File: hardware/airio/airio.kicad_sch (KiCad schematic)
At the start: 21 parts, among them J1 LiPo 1S, J2 GPS, J3 SCREEN, J4 I2C, SW1 TS-1187A-B-A-B, U1 XIAO nRF52840 Plus, U2 BMP581, U3 LSM6DSV16X

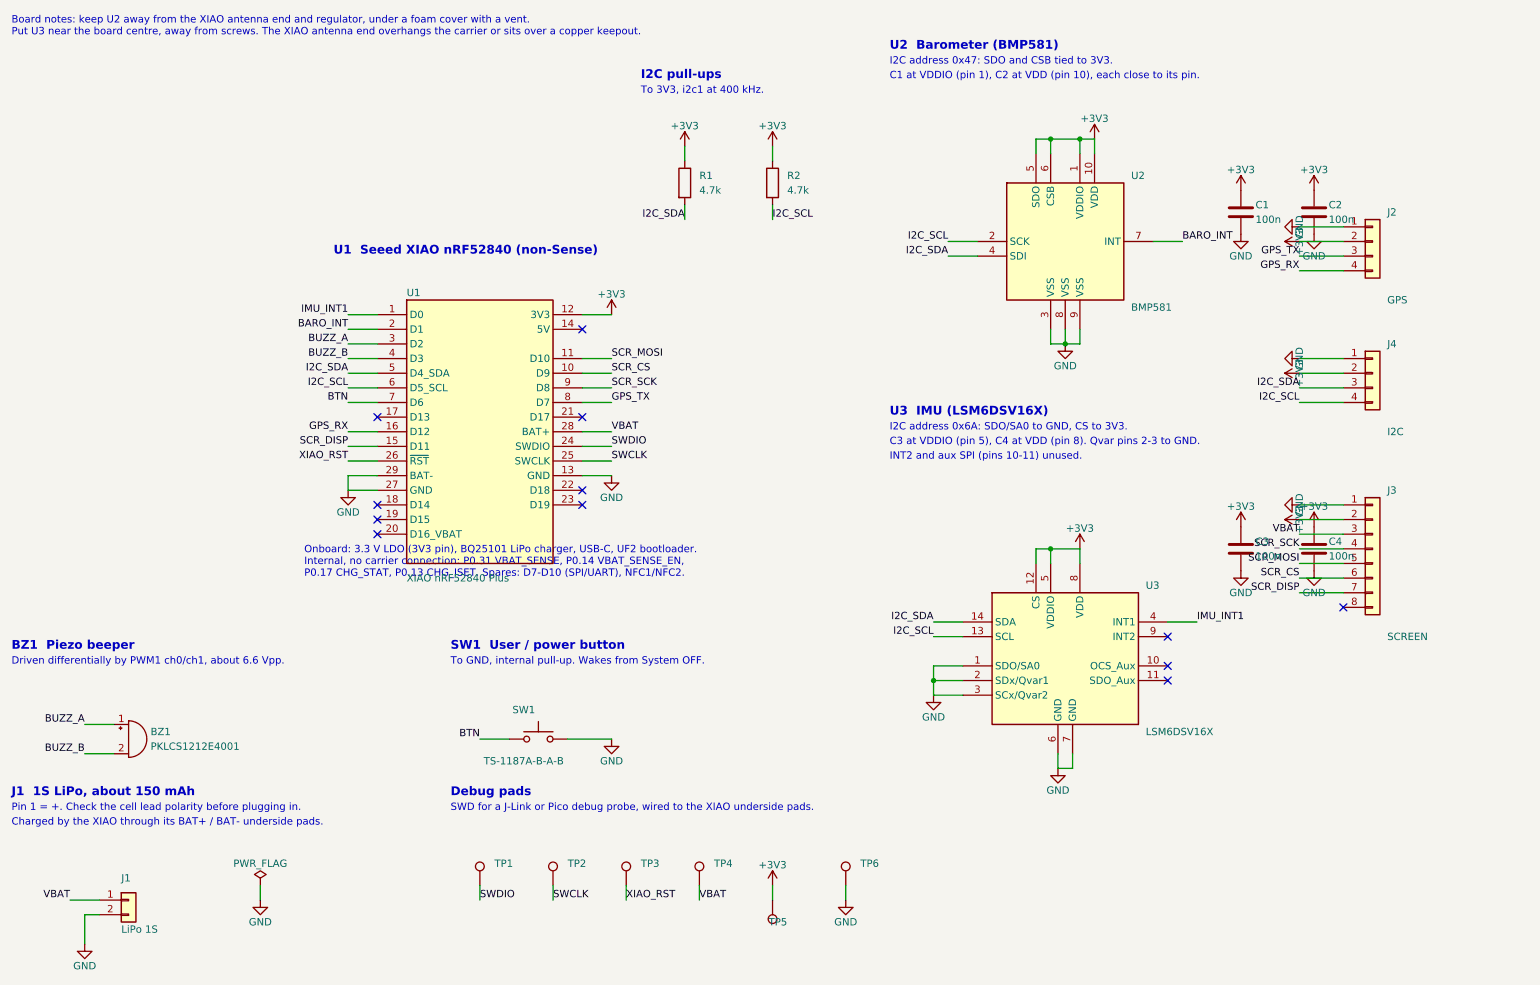
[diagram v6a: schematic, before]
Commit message: airio: back to the standard XIAO, add a TCA9534 I/O expander
- U1 is the standard XIAO nRF52840 again (on LCSC, JLC can place it).
- GPS_RX moves to D1; D6 becomes EXP_INT from the expander.
- U4 TCA9534PWR at 0x20 carries BTN (P0, R4 pull-up), BARO_INT (P1) and
  SCR_DISP (P2); its open-drain INT (R3 pull-up) still wakes the XIAO
  from System OFF. C5 decouples it. NFC pads unused.
- Board: U1 swapped back, U4/R3/R4/C5 placed near the sensors.
- ERC 0 errors; DRC with schematic parity has no footprint errors.
- Pin map and parts tables updated.

Co-Authored-By: Claude Opus 5.5 (1M context) <noreply@anthropic.com>
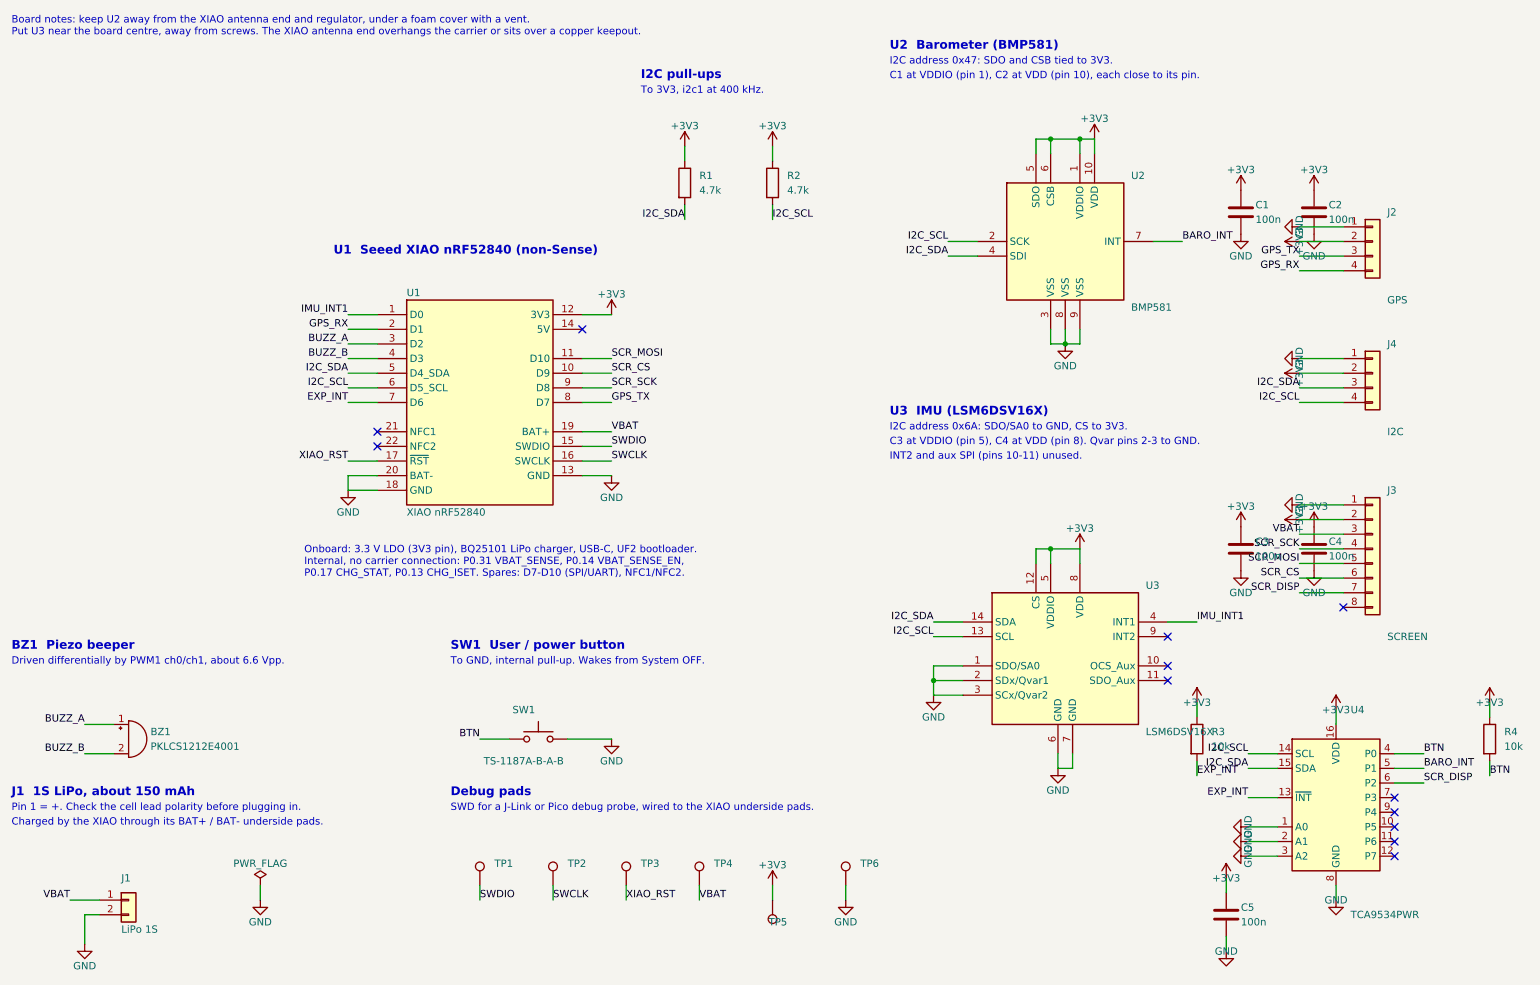
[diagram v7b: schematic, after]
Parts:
- added C5: 100n, Capacitor_SMD:C_0603_1608Metric, symbol Device:C
- added R3, R4: 10k, Resistor_SMD:R_0603_1608Metric, symbol Device:R
- added U4: TCA9534PWR, Package_SO:TSSOP-16_4.4x5mm_P0.65mm, symbol Interface_Expansion:TCA9534
- U1: value XIAO nRF52840 Plus -> XIAO nRF52840; footprint airio:XIAO-nRF52840-Plus-SMD -> airio:XIAO-nRF52840-SMD; symbol airio:XIAO_nRF52840_Plus -> airio:XIAO_nRF52840; LCSC (none) -> C17209540; MPN Seeed 102010672 -> Seeed 102010448; Note Castellated module, soldered flat. Not on LCSC: buy from Se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 -> Castellated module, soldered flat. Seeed SMD footprint.
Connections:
- net +3V3: now also C5.1, R3.1, R4.1, U4.16 (VDD)
- net BARO_INT: now also U4.5 (P1); no longer U1.2 (D1)
- net BTN: now also R4.2, U4.4 (P0); no longer U1.7 (D6)
- net GND: now also U1.18 (GND), U1.20 (BAT-), C5.2, U4.1 (A0), U4.2 (A1), U4.3 (A2), U4.8 (GND); no longer U1.27 (GND), U1.29 (BAT-)
- net GPS_RX: now also U1.2 (D1); no longer U1.16 (D12)
- net I2C_SCL: now also U4.14 (SCL)
- net I2C_SDA: now also U4.15 (SDA)
- net SCR_DISP: now also U4.6 (P2); no longer U1.15 (D11)
- net SWCLK: now also U1.16 (SWCLK); no longer U1.25 (SWCLK)
- net SWDIO: now also U1.15 (SWDIO); no longer U1.24 (SWDIO)
- net VBAT: now also U1.19 (BAT+); no longer U1.28 (BAT+)
- net XIAO_RST: now also U1.17 (~{RST}); no longer U1.26 (~{RST})
- new net EXP_INT: R3.2, U1.7 (D6), U4.13 (~{INT})

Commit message: airio: JST SH ports, off-board buzzer, new pin assignment
- J2/J4 SM04B-SRSS-TB and J3 SM08B-SRSS-TB (JST SH, side-entry SMD) replace
  the PH through-hole headers; J1 battery stays JST PH.
- J5 SM02B-SRSS-TB buzzer port replaces the onboard piezo BZ1.
- Max's pin reassignment for easier routing: SPI on D0-D2, I2C on D3/D4,
  EXP_INT on D5, GPS UART on D7/D8, buzzer on D9/D10; D6 spare.
- IMU_INT1 moves to expander P3; SCR_CLK label renamed SCR_SCK so the
  screen clock reaches J3.
- Includes Max's hand placement and routing in progress.
- ERC 0 errors; DRC with schematic parity has no footprint errors.

Co-Authored-By: Claude Opus 5.5 (1M context) <noreply@anthropic.com>
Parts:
- J2, J4: footprint Connector_JST:JST_PH_B4B-PH-K_1x04_P2.00mm_Vertical -> Connector_JST:JST_SH_SM04B-SRSS-TB_1x04-1MP_P1.00mm_Horizontal; LCSC C131334 -> C160404; MPN JST B4B-PH-K-S(LF)(SN) -> JST SM04B-SRSS-TB(LF)(SN)
- J3: footprint Connector_JST:JST_PH_B8B-PH-K_1x08_P2.00mm_Vertical -> Connector_JST:JST_SH_SM08B-SRSS-TB_1x08-1MP_P1.00mm_Horizontal; LCSC C157974 -> C160407; MPN JST B8B-PH-K-S(LF)(SN) -> JST SM08B-SRSS-TB(LF)(SN)
- J5: renamed from BZ1; value PKLCS1212E4001 -> Buzzer; footprint Buzzer_Beeper:Buzzer_Murata_PKLCS1212E -> Connector_JST:JST_SH_SM02B-SRSS-TB_1x02-1MP_P1.00mm_Horizontal; symbol Device:Buzzer -> Connector_Generic:Conn_01x02; LCSC C113159 -> C160402; MPN Murata PKLCS1212E4001-R1 -> JST SM02B-SRSS-TB(LF)(SN)
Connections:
- net BUZZ_A: now also U1.11 (D10); no longer U1.3 (D2)
- net BUZZ_B: now also U1.10 (D9); no longer U1.4 (D3)
- net EXP_INT: now also U1.6 (D5_SCL); no longer U1.7 (D6)
- net GPS_RX: now also U1.8 (D7); no longer U1.2 (D1)
- net GPS_TX: now also U1.9 (D8); no longer U1.8 (D7)
- net I2C_SCL: now also U1.5 (D4_SDA); no longer U1.6 (D5_SCL)
- net I2C_SDA: now also U1.4 (D3); no longer U1.5 (D4_SDA)
- net IMU_INT1: now also U4.7 (P3); no longer U1.1 (D0)
- net SCR_CS: now also U1.3 (D2); no longer U1.10 (D9)
- net SCR_MOSI: now also U1.1 (D0); no longer U1.11 (D10)
- net SCR_SCK: now also U1.2 (D1); no longer U1.9 (D8)
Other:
- moved on the sheet: J5
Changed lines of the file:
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@@
 	)
 	(no_connect
-		(at 260.35 162.56)
-	)
-	(no_connect
 		(at 83.82 101.6)
 	)
@@
 		(at 260.35 167.64)
 	)
+	(no_connect
+		(at 83.82 93.98)
+	)
 	(wire
 		(pts
@@
 	(wire
 		(pts
-			(xy 83.82 93.98) (xy 78.74 93.98)
-		)
-		(stroke
-			(width 0)
-			(type default)
-		)
-	)
-	(wire
-		(pts
 			(xy 119.38 78.74) (xy 124.46 78.74)
 		)
@@
 	(wire
 		(pts
+			(xy 260.35 162.56) (xy 265.43 162.56)
+		)
+		(stroke
+			(width 0)
+			(type default)
+		)
+	)
+	(wire
+		(pts
 			(xy 33.02 182.88) (xy 33.02 187.96)
 		)
@@
 	(wire
 		(pts
+			(xy 38.1 152.4) (xy 38.1 154.94)
+		)
+		(stroke
+			(width 0)
+			(type default)
+		)
+	)
+	(wire
+		(pts
 			(xy 152.4 52.07) (xy 152.4 49.53)
 		)
@@
 		)
 	)
-	(label "EXP_INT"
-		(at 78.74 93.98 180)
-		(effects
-			(font
-				(size 1.27 1.27)
-			)
-			(justify right bottom)
-		)
-	)
 	(label "BARO_INT"
 		(at 265.43 157.48 0)
@@
 		)
 	)
-	(label "BUZZ_B"
+	(label "IMU_INT1"
+		(at 265.43 162.56 0)
+		(effects
+			(font
+				(size 1.27 1.27)
+			)
+			(justify left bottom)
+		)
+	)
+	(label "I2C_SDA"
 		(at 78.74 86.36 180)
 		(effects
@@
 		)
 	)
-	(label "SCR_SCK"
+	(label "GPS_TX"
 		(at 124.46 91.44 0)
 		(effects
@@
 		)
 	)
-	(label "SCR_MOSI"
+	(label "BUZZ_A"
 		(at 124.46 86.36 0)
 		(effects
@@
 		)
 	)
-	(label "SCR_CS"
+	(label "BUZZ_B"
 		(at 124.46 88.9 0)
 		(effects
@@
 		)
 	)
-	(label "I2C_SDA"
+	(label "I2C_SCL"
 		(at 78.74 88.9 180)
 		(effects
@@
 		)
 	)
-	(label "I2C_SCL"
+	(label "EXP_INT"
 		(at 78.74 91.44 180)
 		(effects
@@
 		)
 	)
-	(label "IMU_INT1"
+	(label "SCR_MOSI"
 		(at 78.74 78.74 180)
 		(effects
@@
 		)
 	)
-	(label "BUZZ_A"
+	(label "SCR_CS"
 		(at 78.74 83.82 180)
 		(effects
@@
 		)
 	)
-	(label "GPS_RX"
+	(label "SCR_SCK"
 		(at 78.74 81.28 180)
 		(effects
@@
 		)
 	)
-	(label "GPS_TX"
+	(label "GPS_RX"
 		(at 124.46 93.98 0)
 		(effects
@@
 			)
 		)
-		(property "Footprint" "Connector_JST:JST_PH_B8B-PH-K_1x08_P2.00mm_Vertical"
+		(property "Footprint" "Connector_JST:JST_SH_SM08B-SRSS-TB_1x08-1MP_P1.00mm_Horizontal"
 			(at 256.54 119.38 0)
 			(hide yes)
@@
 			)
 		)
-		(property "LCSC" "C157974"
+		(property "LCSC" "C160407"
 			(at 256.54 119.38 0)
 			(hide yes)
@@
 			)
 		)
-		(property "MPN" "JST B8B-PH-K-S(LF)(SN)"
+		(property "MPN" "JST SM08B-SRSS-TB(LF)(SN)"
 			(at 256.54 119.38 0)
 			(hide yes)
@@
 			)
 		)
-		(property "Footprint" "Connector_JST:JST_PH_B4B-PH-K_1x04_P2.00mm_Vertical"
+		(property "Footprint" "Connector_JST:JST_SH_SM04B-SRSS-TB_1x04-1MP_P1.00mm_Horizontal"
 			(at 256.54 88.9 0)
 			(hide yes)
@@
 			)
 		)
-		(property "LCSC" "C131334"
+		(property "LCSC" "C160404"
 			(at 256.54 88.9 0)
 			(hide yes)
@@
 			)
 		)
-		(property "MPN" "JST B4B-PH-K-S(LF)(SN)"
+		(property "MPN" "JST SM04B-SRSS-TB(LF)(SN)"
 			(at 256.54 88.9 0)
 			(hide yes)
@@
 	)
 	(symbol
-		(lib_id "Device:Buzzer")
-		(at 40.64 152.4 0)
+		(lib_id "Connector_Generic:Conn_01x02")
+		(at 43.18 149.86 0)
 		(unit 1)
 		(body_style 1)
@@
 		(in_pos_files yes)
 		(dnp no)
-		(property "Reference" "BZ1"
-			(at 44.45 151.13 0)
+		(property "Reference" "J5"
+			(at 41.91 146.05 0)
 			(show_name no)
 			(do_not_autoplace no)
@@
 			)
 		)
-		(property "Value" "PKLCS1212E4001"
-			(at 44.45 153.67 0)
+		(property "Value" "Buzzer"
+			(at 41.91 156.21 0)
 			(show_name no)
 			(do_not_autoplace no)
@@
 			)
 		)
-		(property "Footprint" "Buzzer_Beeper:Buzzer_Murata_PKLCS1212E"
-			(at 40.64 152.4 0)
+		(property "Footprint" "Connector_JST:JST_SH_SM02B-SRSS-TB_1x02-1MP_P1.00mm_Horizontal"
+			(at 43.18 149.86 0)
 			(hide yes)
 			(show_name no)
@@
 		)
 		(property "Datasheet" ""
-			(at 40.64 152.4 0)
+			(at 43.18 149.86 0)
 			(hide yes)
 			(show_name no)
@@
 		)
 		(property "Description" ""
-			(at 40.64 152.4 0)
+			(at 43.18 149.86 0)
 			(show_name no)
 			(do_not_autoplace no)
@@
 			)
 		)
-		(property "LCSC" "C113159"
-			(at 40.64 152.4 0)
+		(property "LCSC" "C160402"
+			(at 43.18 149.86 0)
 			(hide yes)
 			(show_name no)
@@
 			)
 		)
-		(property "MPN" "Murata PKLCS1212E4001-R1"
-			(at 40.64 152.4 0)
+		(property "MPN" "JST SM02B-SRSS-TB(LF)(SN)"
+			(at 43.18 149.86 0)
 			(hide yes)
 			(show_name no)
@@
 			(project "airio"
 				(path "/4be64db2-d0eb-44ab-9167-6be2786d9585"
-					(reference "BZ1")
+					(reference "J5")
 					(unit 1)
 				)
@@
 			)
 		)
-		(property "Footprint" "Connector_JST:JST_PH_B4B-PH-K_1x04_P2.00mm_Vertical"
+		(property "Footprint" "Connector_JST:JST_SH_SM04B-SRSS-TB_1x04-1MP_P1.00mm_Horizontal"
 			(at 256.54 66.04 0)
 			(hide yes)
@@
 			)
 		)
-		(property "LCSC" "C131334"
+		(property "LCSC" "C160404"
 			(at 256.54 66.04 0)
 			(hide yes)
@@
 			)
 		)
-		(property "MPN" "JST B4B-PH-K-S(LF)(SN)"
+		(property "MPN" "JST SM04B-SRSS-TB(LF)(SN)"
 			(at 256.54 66.04 0)
 			(hide yes)
